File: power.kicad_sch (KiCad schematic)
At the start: 119 parts, among them J6 Molex_Nano-Fit_1x2_105309-2202, Q1 BSS138-7-F, Q13 MMBT3904LT1G, Q14 MMBT3904LT1G, Q2 SI7613DN-T1-GE3, Q3 BSS138-7-F, Q4 SI7613DN-T1-GE3, U18 TPS56C230, U19 TPS56C230, U20 TPS3840PL30DBVR, U21 TPS564247DRLR, U22 TPS564247DRLR, U23 TLV73333PDBVT, U48 INA219AIDCNR, U49 INA219AIDCNR, U50 INA219AIDCNR

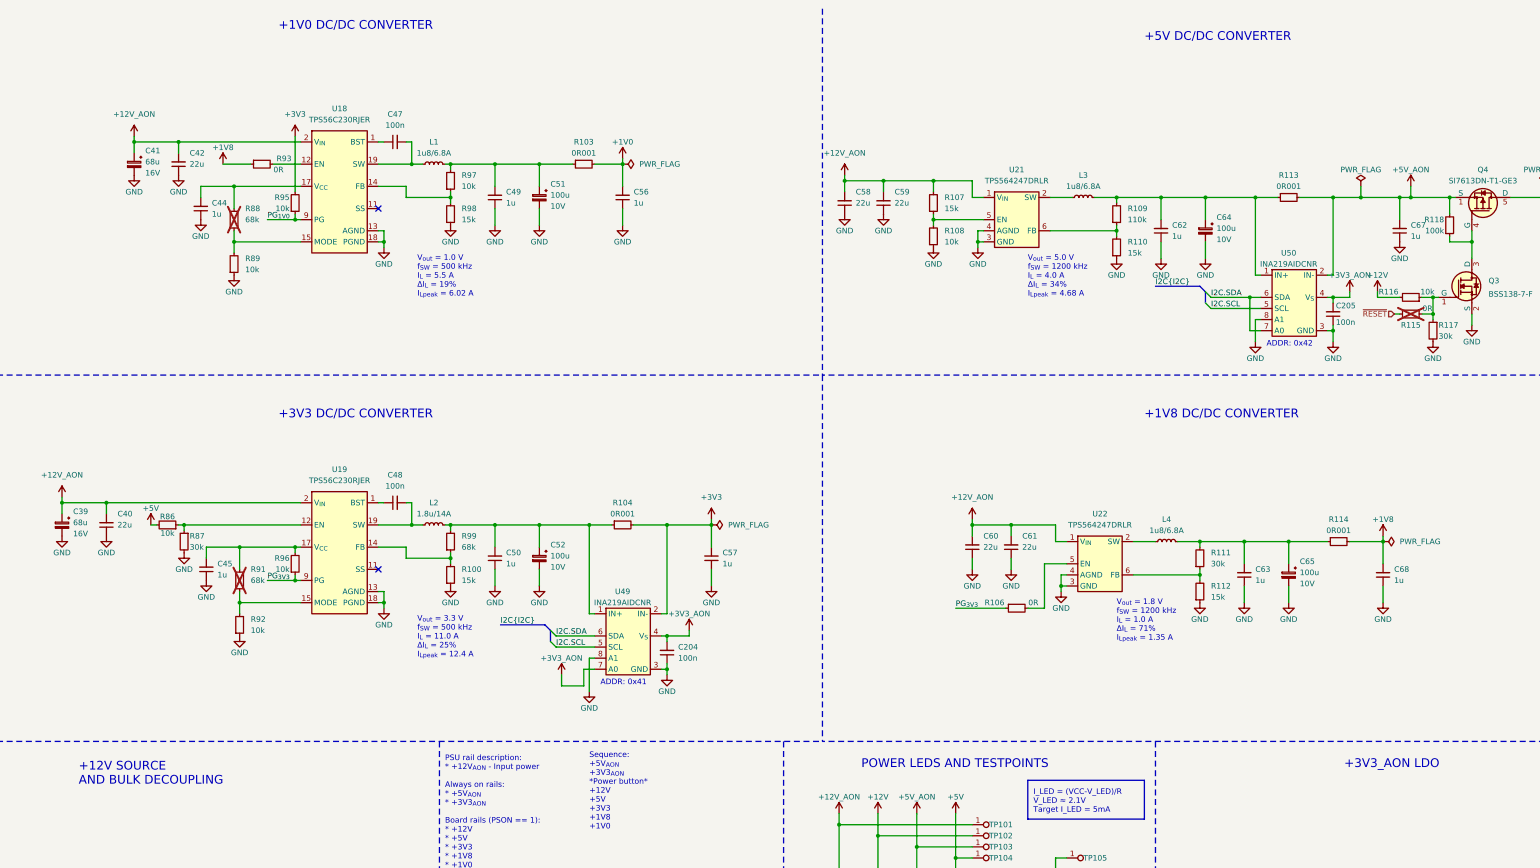
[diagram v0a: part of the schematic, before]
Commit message: [#70030] Unify functional block names
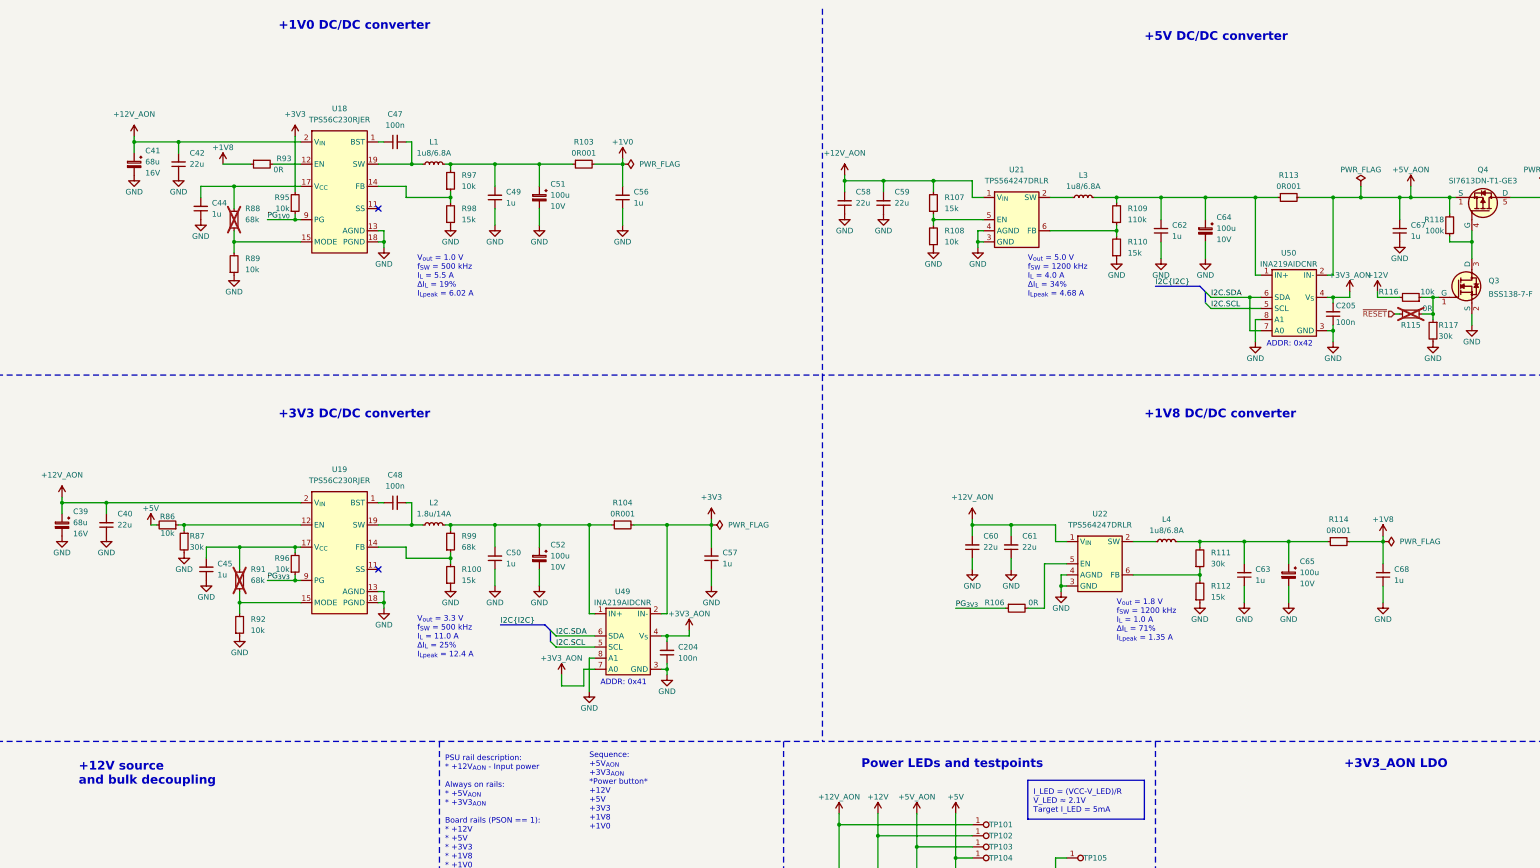
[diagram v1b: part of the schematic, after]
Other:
- note added: "+12V source and bulk decoupling"
- note added: "+1V0 DC/DC converter"
- note added: "+1V8 DC/DC converter"
- note added: "+3V3 DC/DC converter"
- note added: "+5V DC/DC converter"
- note added: "Power LEDs and testpoints"
- note removed: "+12V SOURCE AND BULK DECOUPLING"
- note removed: "+1V0 DC/DC CONVERTER"
- note removed: "+1V8 DC/DC CONVERTER"
- note removed: "+3V3 DC/DC CONVERTER"
- note removed: "+5V DC/DC CONVERTER"
- note removed: "POWER LEDS AND TESTPOINTS"
- company: Antmicro Ltd. -> Antmicro Ltd
- title: Com Express 7 baseboard -> COM Express 7 Baseboard
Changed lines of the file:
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@@
 	(paper "A3")
 	(title_block
-		(title "Com Express 7 baseboard")
-		(date "2024-03-28")
+		(title "COM Express 7 Baseboard")
+		(date "2024-12-13")
 		(rev "1.1.0")
-		(company "Antmicro Ltd.")
+		(company "Antmicro Ltd")
+		(comment 1 "www.antmicro.com")
 	)
 	(junction
@@
 			(font
 				(size 2 2)
+				(thickness 0.4)
+				(bold yes)
 			)
 			(justify left bottom)
@@
 		)
 	)
-	(text "+12V SOURCE\nAND BULK DECOUPLING"
+	(text "+12V source\nand bulk decoupling"
 		(exclude_from_sim no)
 		(at 53.34 190.5 0)
@@
 			(font
 				(size 2 2)
+				(thickness 0.4)
+				(bold yes)
 			)
 			(justify left bottom)
@@
 		)
 	)
-	(text "+1V0 DC/DC CONVERTER"
+	(text "+1V0 DC/DC converter"
 		(exclude_from_sim no)
 		(at 99.06 17.78 0)
@@
 			(font
 				(size 2 2)
+				(thickness 0.4)
+				(bold yes)
 			)
 			(justify left bottom)
@@
 		)
 	)
-	(text "+5V DC/DC CONVERTER"
+	(text "+5V DC/DC converter"
 		(exclude_from_sim no)
 		(at 297.18 20.32 0)
@@
 			(font
 				(size 2 2)
+				(thickness 0.4)
+				(bold yes)
 			)
 			(justify left bottom)
@@
 		)
 	)
-	(text "+1V8 DC/DC CONVERTER"
+	(text "+1V8 DC/DC converter"
 		(exclude_from_sim no)
 		(at 297.18 106.68 0)
@@
 			(font
 				(size 2 2)
+				(thickness 0.4)
+				(bold yes)
 			)
 			(justify left bottom)
@@
 		)
 	)
-	(text "+3V3 DC/DC CONVERTER"
+	(text "+3V3 DC/DC converter"
 		(exclude_from_sim no)
 		(at 99.06 106.68 0)
@@
 			(font
 				(size 2 2)
+				(thickness 0.4)
+				(bold yes)
 			)
 			(justify left bottom)
 		)
 	)
-	(text "POWER LEDS AND TESTPOINTS"
+	(text "Power LEDs and testpoints"
 		(exclude_from_sim no)
 		(at 232.41 186.69 0)
@@
 			(font
 				(size 2 2)
+				(thickness 0.4)
+				(bold yes)
 			)
 			(justify left bottom)

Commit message: [#69944] Fix power button and autostartup on the schematic
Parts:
- added D36: BAT54C, antmicro-footprints:SOT-23-3, symbol antmicroDiodesRectifiersSingle:BAT54C
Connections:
- net PSON: now also D36.3
- net at R86.1, R87.1, U19.12 (EN): now also D36.1, D36.2
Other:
- moved on the sheet: C204, C39, C40, C41, C42, C44, C45, C47, C48, C49, C50, C51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

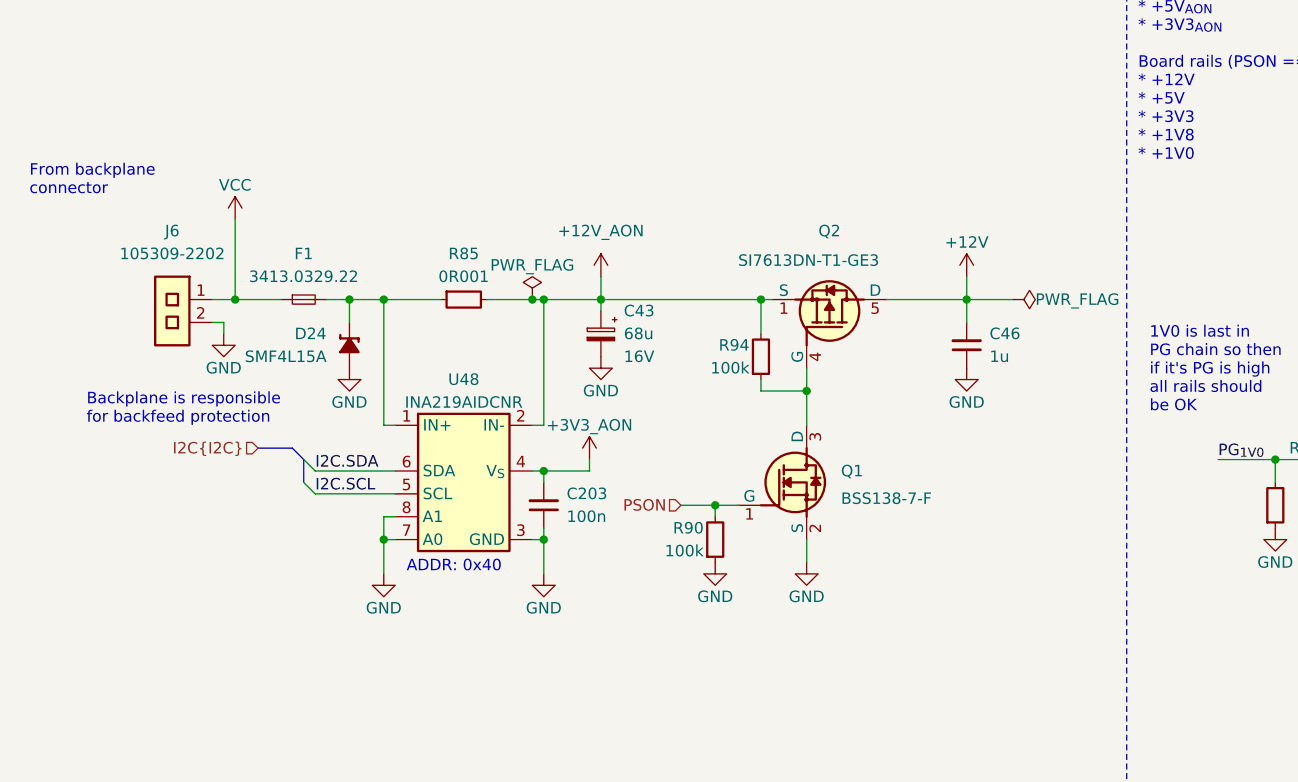
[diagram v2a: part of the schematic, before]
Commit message: [#70532] Change Molex Nano-Fit connector from 105309-2202 to 105309-1202
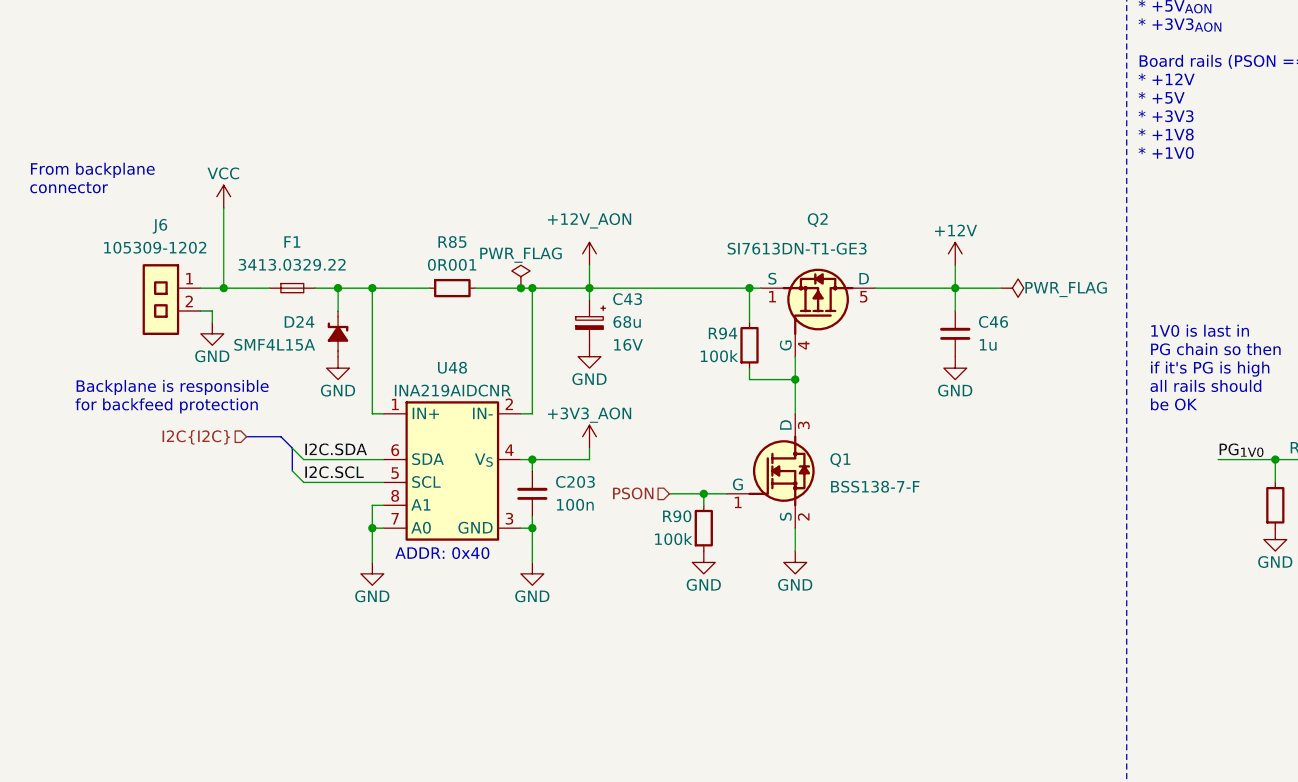
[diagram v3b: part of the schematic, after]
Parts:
- removed J6: Molex_Nano-Fit_1x2_105309-2202, antmicro-footprints:Conn_Molex_Nano-Fit_1x2_105309-2202, symbol antmicroWire2BoardConnectors:Molex_Nano-Fit_1x2_105309-2202
- added J6: Molex_Nano-Fit_1x2_105309-1202, antmicro-footprints:Conn_Molex_Nano-Fit_1x2_105309-1202, symbol antmicroWire2BoardConnectors:Molex_Nano-Fit_1x2_105309-1202
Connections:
- net GND: now also J6.2
- net VCC: now also J6.1
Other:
- moved on the sheet: C203, C43, C46, D24, F1, Q1, Q2, R85, R90, R94, U48
